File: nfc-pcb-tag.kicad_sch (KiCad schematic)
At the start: 19 parts, among them IC1 NT3H2111W0FHKH, J1 Conn_ARM_SWD_TagConnect_TC203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, U1 CH32V003FxUx

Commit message: Tweak firmware
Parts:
- removed C3, C4, C5: C, Capacitor_SMD:C_0402_1005Metric, symbol Device:C
- removed D2: LED, LED_SMD:LED_0402_1005Metric, symbol Device:LED
- removed R6: 1k, Resistor_SMD:R_0402_1005Metric, symbol Device:R
- added C6, C7: C, Capacitor_SMD:C_0402_1005Metric, symbol Device:C
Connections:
- net +3.3V: now also C6.1, C7.1
- net A0: now also U1.20 (PD6); no longer U1.19 (PD5)
- net A1: now also U1.19 (PD5); no longer U1.20 (PD6)
- net GND: now also U1.12 (PC5), C6.2, C7.2
- net at C1.2, IC1.1 (LA), TP3.2: now also C1.1, IC1.8 (LB), TP3.1
- net RST: no longer names the net of U1.1 (PD7)
- net RST: no longer J1.3 (~{RESET})
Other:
- note added: "This bridge ensures we can make the spiral trace connect"

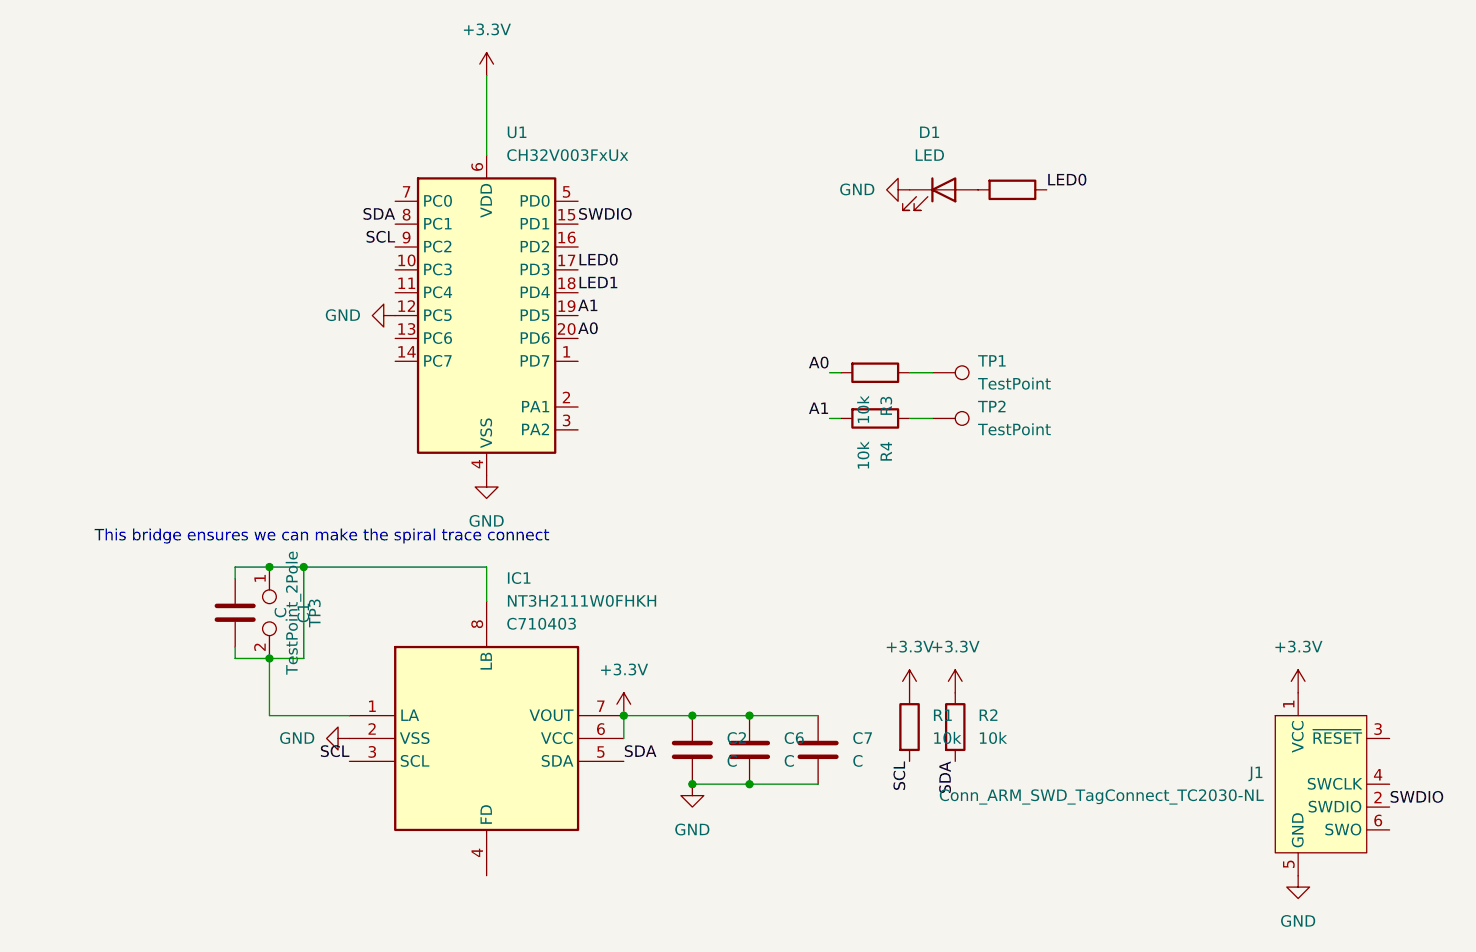
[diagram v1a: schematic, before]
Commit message: Convert to inductor antenna
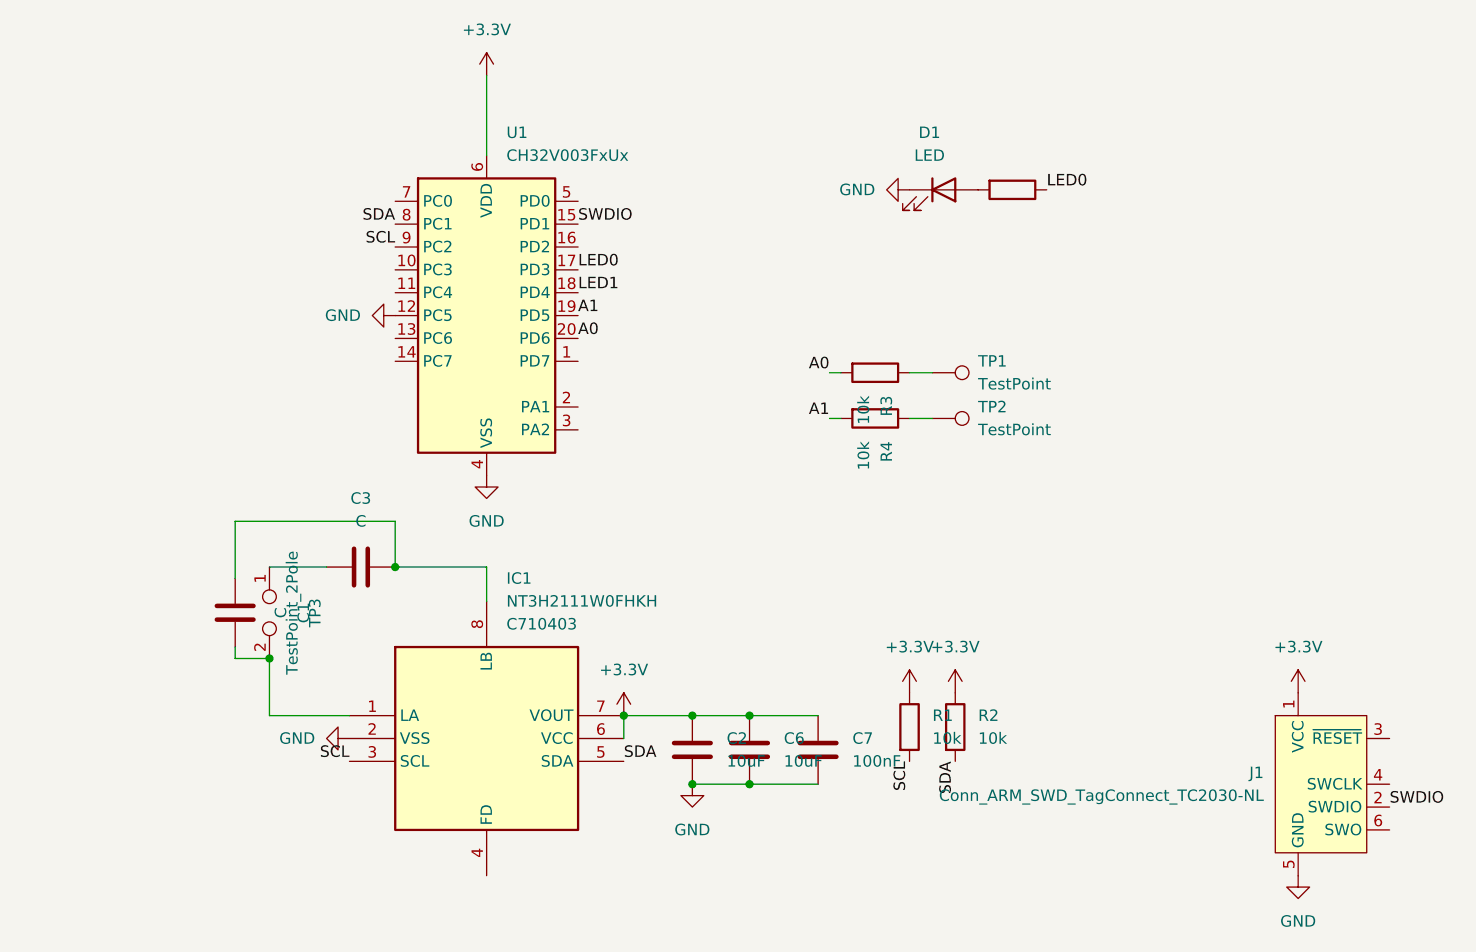
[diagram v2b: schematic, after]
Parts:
- added C3: C, Capacitor_SMD:C_0402_1005Metric, symbol Device:C
- C1: footprint Capacitor_SMD:C_0603_1608Metric -> Capacitor_SMD:C_0402_1005Metric
- C2, C6: value C -> 10uF; LCSC Part (none) -> C15525
- C7: value C -> 100nF; LCSC Part (none) -> C541406
- D1: LCSC Part (none) -> C5336761
- R1, R2, R3, R4: LCSC Part (none) -> C60490
- R5: LCSC Part (none) -> C114759
- TP3: footprint (none) -> Library:ANT; LCSC Part (none) -> C33126958
- U1: LCSC Part (none) -> C5299908
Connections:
- net at C1.2, IC1.1 (LA), TP3.2: no longer C1.1, IC1.8 (LB), TP3.1
- new net: C1.1, C3.2, IC1.8 (LB)
- new net: C3.1, TP3.1
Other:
- note removed: "This bridge ensures we can make the spiral trace connect"
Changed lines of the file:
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@@
 	(paper "A4")
-	(junction
-		(at 35.56 83.82)
-		(diameter 0)
-		(color 0 0 0 0)
-	)
 	(junction
 		(at 88.9 107.95)
@@
 	)
 	(junction
-		(at 39.37 83.82)
+		(at 49.53 83.82)
 		(diameter 0)
 		(color 0 0 0 0)
@@
 	(wire
 		(pts
-			(xy 39.37 83.82) (xy 59.69 83.82)
+			(xy 35.56 83.82) (xy 41.91 83.82)
 		)
 		(stroke
@@
 	(wire
 		(pts
-			(xy 31.75 83.82) (xy 31.75 85.09)
+			(xy 31.75 78.74) (xy 31.75 85.09)
 		)
 		(stroke
@@
 	(wire
 		(pts
-			(xy 35.56 83.82) (xy 31.75 83.82)
+			(xy 31.75 78.74) (xy 49.53 78.74)
 		)
 		(stroke
@@
 	(wire
 		(pts
-			(xy 35.56 93.98) (xy 39.37 93.98)
+			(xy 35.56 93.98) (xy 31.75 93.98)
 		)
 		(stroke
@@
 	(wire
 		(pts
-			(xy 35.56 93.98) (xy 31.75 93.98)
+			(xy 49.53 83.82) (xy 49.53 78.74)
 		)
 		(stroke
@@
 	(wire
 		(pts
-			(xy 39.37 93.98) (xy 39.37 83.82)
+			(xy 35.56 100.33) (xy 35.56 93.98)
 		)
 		(stroke
@@
 	(wire
 		(pts
-			(xy 35.56 83.82) (xy 39.37 83.82)
+			(xy 49.53 83.82) (xy 59.69 83.82)
 		)
 		(stroke
 			(width 0)
 			(type default)
-		)
-	)
-	(wire
-		(pts
-			(xy 35.56 100.33) (xy 35.56 93.98)
-		)
-		(stroke
-			(width 0)
-			(type default)
-		)
-	)
-	(text "This bridge ensures we can make the spiral trace connect"
-		(exclude_from_sim no)
-		(at 41.402 80.518 0)
-		(effects
-			(font
-				(size 1.27 1.27)
-			)
 		)
 	)
@@
 			)
 		)
+		(property "LCSC Part" "C60490"
+			(at 106.68 101.6 0)
+			(effects
+				(font
+					(size 1.27 1.27)
+				)
+				(hide yes)
+			)
+		)
 		(pin "1"
 		)
@@
 	)
 	(symbol
+		(lib_id "Device:C")
+		(at 45.72 83.82 90)
+		(unit 1)
+		(exclude_from_sim no)
+		(in_bom yes)
+		(on_board yes)
+		(dnp no)
+		(fields_autoplaced yes)
+		(property "Reference" "C3"
+			(at 45.72 76.2 90)
+			(effects
+				(font
+					(size 1.27 1.27)
+				)
+			)
+		)
+		(property "Value" "C"
+			(at 45.72 78.74 90)
+			(effects
+				(font
+					(size 1.27 1.27)
+				)
+			)
+		)
+		(property "Footprint" "Capacitor_SMD:C_0402_1005Metric"
+			(at 49.53 82.8548 0)
+			(effects
+				(font
+					(size 1.27 1.27)
+				)
+				(hide yes)
+			)
+		)
+		(property "Datasheet" "~"
+			(at 45.72 83.82 0)
+			(effects
+				(font
+					(size 1.27 1.27)
+				)
+				(hide yes)
+			)
+		)
+		(property "Description" "Unpolarized capacitor"
+			(at 45.72 83.82 0)
+			(effects
+				(font
+					(size 1.27 1.27)
+				)
+				(hide yes)
+			)
+		)
+		(property "LCSC Part" "C107010"
+			(at 45.72 83.82 0)
+			(effects
+				(font
+					(size 1.27 1.27)
+				)
+				(hide yes)
+			)
+		)
+		(pin "1"
+		)
+		(pin "2"
+		)
+		(instances
+			(project "nfc-pcb-tag"
+				(path "/af676c0f-31c4-428e-bd52-648c0da860d7"
+					(reference "C3")
+					(unit 1)
+				)
+			)
+		)
+	)
+	(symbol
 		(lib_id "power:+3.3V")
 		(at 74.93 100.33 0)
@@
 			)
 		)
-		(property "Value" "C"
+		(property "Value" "10uF"
 			(at 86.36 105.4099 0)
 			(effects
@@
 			)
 		)
+		(property "LCSC Part" "C15525"
+			(at 82.55 104.14 0)
+			(effects
+				(font
+					(size 1.27 1.27)
+				)
+				(hide yes)
+			)
+		)
 		(pin "2"
 		)
@@
 			)
 		)
-		(property "Value" "C"
+		(property "Value" "10uF"
 			(at 92.71 105.4099 0)
 			(effects
@@
 			)
 		)
+		(property "LCSC Part" "C15525"
+			(at 88.9 104.14 0)
+			(effects
+				(font
+					(size 1.27 1.27)
+				)
+				(hide yes)
+			)
+		)
 		(pin "2"
 		)
@@
 			)
 		)
+		(property "LCSC Part" "C114759 "
+			(at 118.11 41.91 0)
+			(effects
+				(font
+					(size 1.27 1.27)
+				)
+				(hide yes)
+			)
+		)
 		(pin "1"
 		)
@@
 			)
 		)
-		(property "Footprint" "Capacitor_SMD:C_0603_1608Metric"
+		(property "Footprint" "Capacitor_SMD:C_0402_1005Metric"
 			(at 32.7152 92.71 0)
 			(effects
@@
 			)
 		)
+		(property "LCSC Part" "C60490"
+			(at 102.87 67.31 0)
+			(effects
+				(font
+					(size 1.27 1.27)
+				)
+				(hide yes)
+			)
+		)
 		(pin "1"
 		)
@@
 			)
 		)
+		(property "LCSC Part" "C5299908"
+			(at 59.69 55.88 0)
+			(effects
+				(font
+					(size 1.27 1.27)
+				)
+				(hide yes)
+			)
+		)
 		(pin "10"
 		)
@@
 			)
 		)
-		(property "Footprint" ""
+		(property "Footprint" "Library:ANT"
 			(at 35.56 88.9 0)
 			(effects
@@
 			)
 		)
+		(property "LCSC Part" "C33126958"
+			(at 35.56 88.9 0)
+			(effects
+				(font
+					(size 1.27 1.27)
+				)
+				(hide yes)
+			)
+		)
 		(pin "1"
 		)
@@
 			)
 		)
+		(property "LCSC Part" "C60490"
+			(at 111.76 101.6 0)
+			(effects
+				(font
+					(size 1.27 1.27)
+				)
+				(hide yes)
+			)
+		)
 		(pin "1"
 		)
@@
 			)
 		)
-		(property "Value" "C"
+		(property "Value" "100nF"
 			(at 100.33 105.4099 0)
 			(effects
@@
 			)
 		)
+		(property "LCSC Part" "C541406"
+			(at 96.52 104.14 0)
+			(effects
+				(font
+					(size 1.27 1.27)
+				)
+				(hide yes)
+			)
+		)
 		(pin "2"
 		)
@@
 			)
 		)
+		(property "LCSC Part" "C5336761 "
+			(at 110.49 41.91 0)
+			(effects
+				(font
+					(size 1.27 1.27)
+				)
+				(hide yes)
+			)
+		)
 		(pin "2"
 		)
@@
 			(at 102.87 62.23 0)
 			(effects
+				(font
+					(size 1.27 1.27)
+				)
+				(hide yes)
+			)
+		)
+		(property "LCSC Part" "C60490"
+			(at 102.87 62.23 0)
+			(effects

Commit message: Add kibot yaml
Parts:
- C3: value C -> 68p
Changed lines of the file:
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@@
 			)
 		)
-		(property "Value" "C"
+		(property "Value" "68p"
 			(at 45.72 78.74 90)
 			(effects

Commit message: Revise to use buttons
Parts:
- removed R3, R4: 10k, Resistor_SMD:R_0402_1005Metric, symbol Device:R
- removed TP1, TP2: TestPoint, symbol Connector:TestPoint
- added SW1, SW2: SW_Push, Button_Switch_SMD:SW_SPST_B3U-3000P, symbol Switch:SW_Push
- ANT1: renamed from TP3; value TestPoint_2Pole -> ANT
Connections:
- net A0: now also SW1.1
- net A1: now also SW2.1
- net GND: now also SW1.2, SW2.2
